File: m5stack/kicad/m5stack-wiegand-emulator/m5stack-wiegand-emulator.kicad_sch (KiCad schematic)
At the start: 42 parts, among them J1 2x15 socket header, J2 2x15 pin header, J3 1x5 female, T1 TestPoint, T2 TestPoint, T3 TestPoint, T4 TestPoint, U1 RP2040, U2 ISOW7841, U3 SN74LVC2G126-EP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

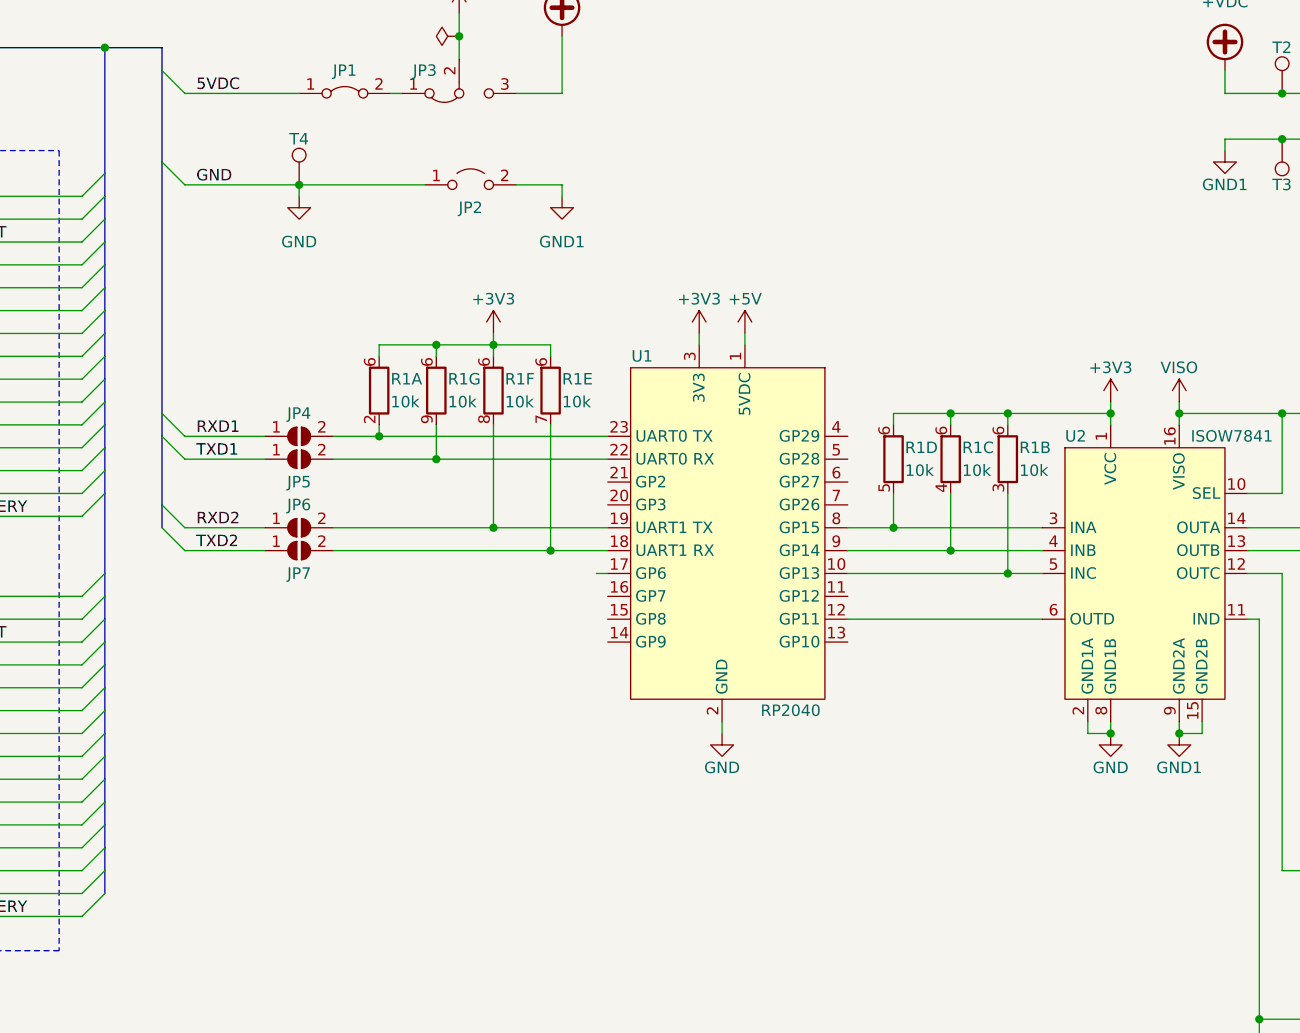
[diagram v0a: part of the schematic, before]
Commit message: M5: moved DI/DO to GP28/29"
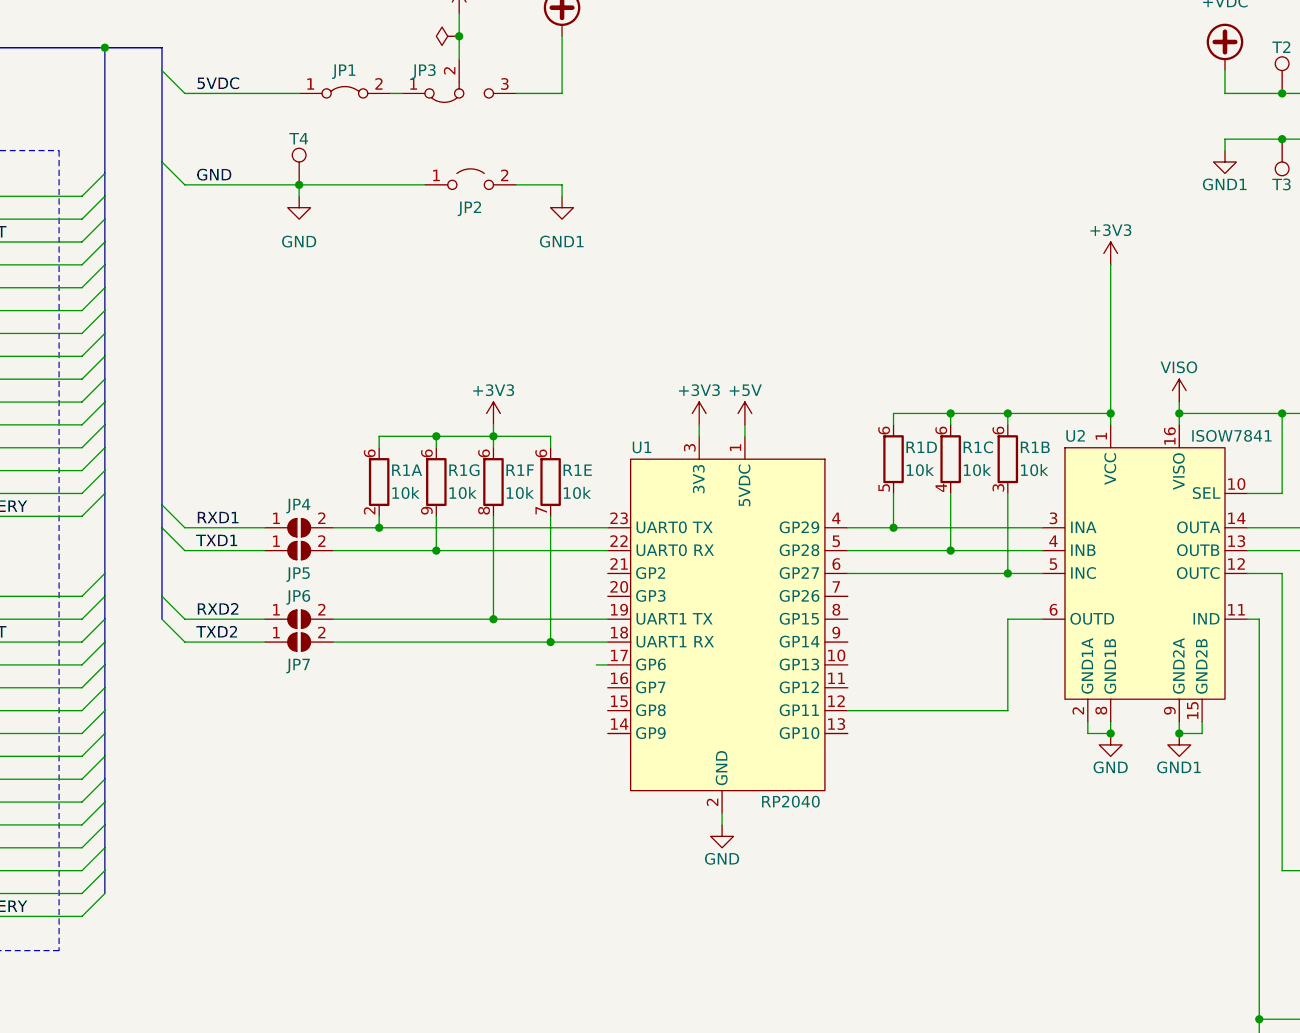
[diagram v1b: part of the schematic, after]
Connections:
- net at R1.4 (R3.2), U2.4 (INB): now also U1.5 (GP28); no longer U1.9 (GP14)
- net at R1.3 (R2.2), U2.5 (INC): now also U1.6 (GP27); no longer U1.10 (GP13)
- net at R1.5 (R4.2), U2.3 (INA): now also U1.4 (GP29); no longer U1.8 (GP15)
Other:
- moved on the sheet: JP4, JP5, JP6, JP7, R1A, R1E, R1F, R1G, U1

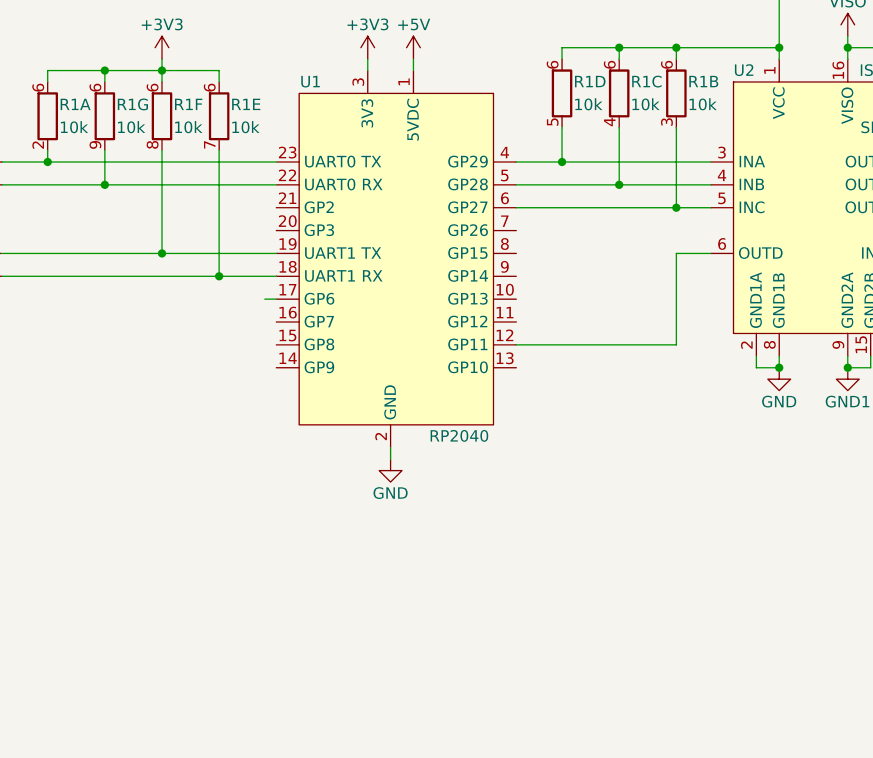
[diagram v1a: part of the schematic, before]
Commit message: M5: routing LED IN signal
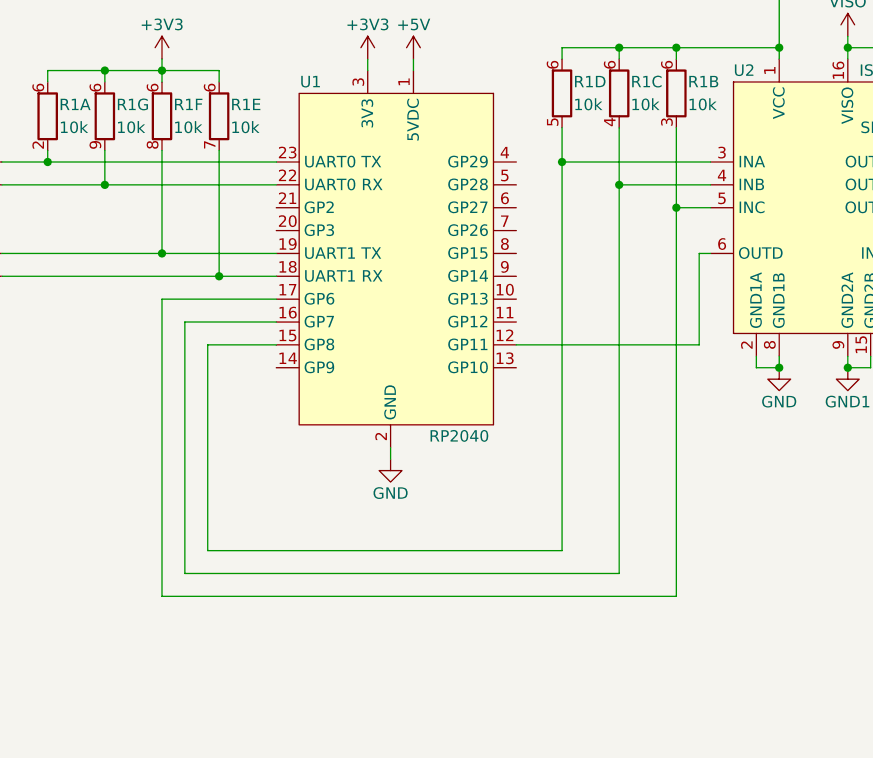
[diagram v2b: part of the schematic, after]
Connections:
- net at R1.4 (R3.2), U2.4 (INB): now also U1.16 (GP7); no longer U1.5 (GP28)
- net at R1.3 (R2.2), U2.5 (INC): now also U1.17 (GP6); no longer U1.6 (GP27)
- net at R1.5 (R4.2), U2.3 (INA): now also U1.15 (GP8); no longer U1.4 (GP29)
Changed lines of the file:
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@@
   (junction (at 233.68 138.43) (diameter 0) (color 0 0 0 0)
   )
+  (junction (at 163.83 88.9) (diameter 0) (color 0 0 0 0)
+  )
   (junction (at 102.87 29.21) (diameter 0) (color 0 0 0 0)
   )
@@
   (junction (at 233.68 148.59) (diameter 0) (color 0 0 0 0)
   )
+  (junction (at 233.68 91.44) (diameter 0) (color 0 0 0 0)
+  )
+  (junction (at 233.68 86.36) (diameter 0) (color 0 0 0 0)
+  )
+  (junction (at 151.13 83.82) (diameter 0) (color 0 0 0 0)
+  )
+  (junction (at 199.39 71.12) (diameter 0) (color 0 0 0 0)
+  )
+  (junction (at 191.77 138.43) (diameter 0) (color 0 0 0 0)
+  )
+  (junction (at 85.09 45.72) (diameter 0) (color 0 0 0 0)
+  )
+  (junction (at 219.71 138.43) (diameter 0) (color 0 0 0 0)
+  )
+  (junction (at 194.31 71.12) (diameter 0) (color 0 0 0 0)
+  )
+  (junction (at 220.98 83.82) (diameter 0) (color 0 0 0 0)
+  )
+  (junction (at 233.68 83.82) (diameter 0) (color 0 0 0 0)
+  )
   (junction (at 157.48 86.36) (diameter 0) (color 0 0 0 0)
   )
-  (junction (at 233.68 91.44) (diameter 0) (color 0 0 0 0)
-  )
-  (junction (at 233.68 86.36) (diameter 0) (color 0 0 0 0)
-  )
-  (junction (at 199.39 71.12) (diameter 0) (color 0 0 0 0)
-  )
-  (junction (at 191.77 138.43) (diameter 0) (color 0 0 0 0)
-  )
-  (junction (at 85.09 45.72) (diameter 0) (color 0 0 0 0)
-  )
-  (junction (at 219.71 138.43) (diameter 0) (color 0 0 0 0)
-  )
-  (junction (at 194.31 71.12) (diameter 0) (color 0 0 0 0)
-  )
-  (junction (at 220.98 83.82) (diameter 0) (color 0 0 0 0)
-  )
-  (junction (at 233.68 83.82) (diameter 0) (color 0 0 0 0)
-  )
   (junction (at 100.33 73.66) (diameter 0) (color 0 0 0 0)
   )
@@
   (junction (at 246.38 138.43) (diameter 0) (color 0 0 0 0)
   )
-  (junction (at 151.13 83.82) (diameter 0) (color 0 0 0 0)
-  )
   (junction (at 106.68 73.66) (diameter 0) (color 0 0 0 0)
   )
   (junction (at 54.61 158.75) (diameter 0) (color 0 0 0 0)
   )
-  (junction (at 163.83 88.9) (diameter 0) (color 0 0 0 0)
-  )
   (bus_entry (at 19.05 93.98) (size 2.54 2.54)
     (stroke (width 0) (type default))
@@
     (stroke (width 0) (type default))
   )
+  (wire (pts (xy 106.68 132.08) (xy 106.68 99.06))
+    (stroke (width 0) (type default))
+  )
   (wire (pts (xy 157.48 71.12) (xy 157.48 72.39))
     (stroke (width 0) (type default))
@@
     (stroke (width 0) (type default))
   )
+  (wire (pts (xy 157.48 129.54) (xy 109.22 129.54))
+    (stroke (width 0) (type default))
+  )
   (wire (pts (xy 157.48 80.01) (xy 157.48 86.36))
     (stroke (width 0) (type default))
@@
     (stroke (width 0) (type default))
   )
-  (wire (pts (xy 119.38 99.06) (xy 118.11 99.06))
+  (wire (pts (xy 106.68 99.06) (xy 119.38 99.06))
     (stroke (width 0) (type default))
   )
@@
     (stroke (width 0) (type default))
   )
+  (wire (pts (xy 163.83 132.08) (xy 106.68 132.08))
+    (stroke (width 0) (type default))
+  )
   (wire (pts (xy 240.03 83.82) (xy 254 83.82))
     (stroke (width 0) (type default))
@@
     (stroke (width 0) (type default))
   )
+  (wire (pts (xy 163.83 88.9) (xy 163.83 132.08))
+    (stroke (width 0) (type default))
+  )
   (wire (pts (xy 219.71 35.56) (xy 222.25 35.56))
     (stroke (width 0) (type default))
   )
+  (wire (pts (xy 111.76 127) (xy 111.76 104.14))
+    (stroke (width 0) (type default))
+  )
   (wire (pts (xy 199.39 78.74) (xy 199.39 88.9))
     (stroke (width 0) (type default))
@@
     (stroke (width 0) (type default))
   )
+  (wire (pts (xy 111.76 104.14) (xy 119.38 104.14))
+    (stroke (width 0) (type default))
+  )
+  (wire (pts (xy 151.13 83.82) (xy 151.13 127))
+    (stroke (width 0) (type default))
+  )
   (wire (pts (xy 182.88 106.68) (xy 185.42 106.68))
     (stroke (width 0) (type default))
@@
     (stroke (width 0) (type default))
   )
-  (wire (pts (xy 163.83 104.14) (xy 163.83 93.98))
+  (wire (pts (xy 166.37 104.14) (xy 166.37 93.98))
     (stroke (width 0) (type default))
   )
@@
     (stroke (width 0) (type default))
   )
-  (wire (pts (xy 163.83 93.98) (xy 167.64 93.98))
+  (wire (pts (xy 166.37 93.98) (xy 167.64 93.98))
     (stroke (width 0) (type default))
   )
@@
     (stroke (width 0) (type default))
   )
+  (wire (pts (xy 157.48 86.36) (xy 157.48 129.54))
+    (stroke (width 0) (type default))
+  )
   (wire (pts (xy 21.59 127) (xy 33.02 127))
     (stroke (width 0) (type default))
@@
     (stroke (width 0) (type default))
   )
-  (wire (pts (xy 146.05 88.9) (xy 163.83 88.9))
-    (stroke (width 0) (type default))
-  )
   (wire (pts (xy 54.61 148.59) (xy 66.04 148.59))
     (stroke (width 0) (type default))
@@
     (stroke (width 0) (type default))
   )
+  (wire (pts (xy 109.22 129.54) (xy 109.22 101.6))
+    (stroke (width 0) (type default))
+  )
   (wire (pts (xy 45.72 93.98) (xy 60.96 93.98))
     (stroke (width 0) (type default))
@@
     (stroke (width 0) (type default))
   )
-  (wire (pts (xy 146.05 86.36) (xy 157.48 86.36))
+  (wire (pts (xy 151.13 127) (xy 111.76 127))
     (stroke (width 0) (type default))
   )
@@
     (stroke (width 0) (type default))
   )
+  (wire (pts (xy 109.22 101.6) (xy 119.38 101.6))
+    (stroke (width 0) (type default))
+  )
   (wire (pts (xy 54.61 148.59) (xy 54.61 151.13))
     (stroke (width 0) (type default))
@@
     (stroke (width 0) (type default))
   )
-  (wire (pts (xy 146.05 104.14) (xy 163.83 104.14))
+  (wire (pts (xy 146.05 104.14) (xy 166.37 104.14))
     (stroke (width 0) (type default))
   )
@@
     (stroke (width 0) (type default))
   )
-  (wire (pts (xy 146.05 83.82) (xy 151.13 83.82))
-    (stroke (width 0) (type default))
-  )

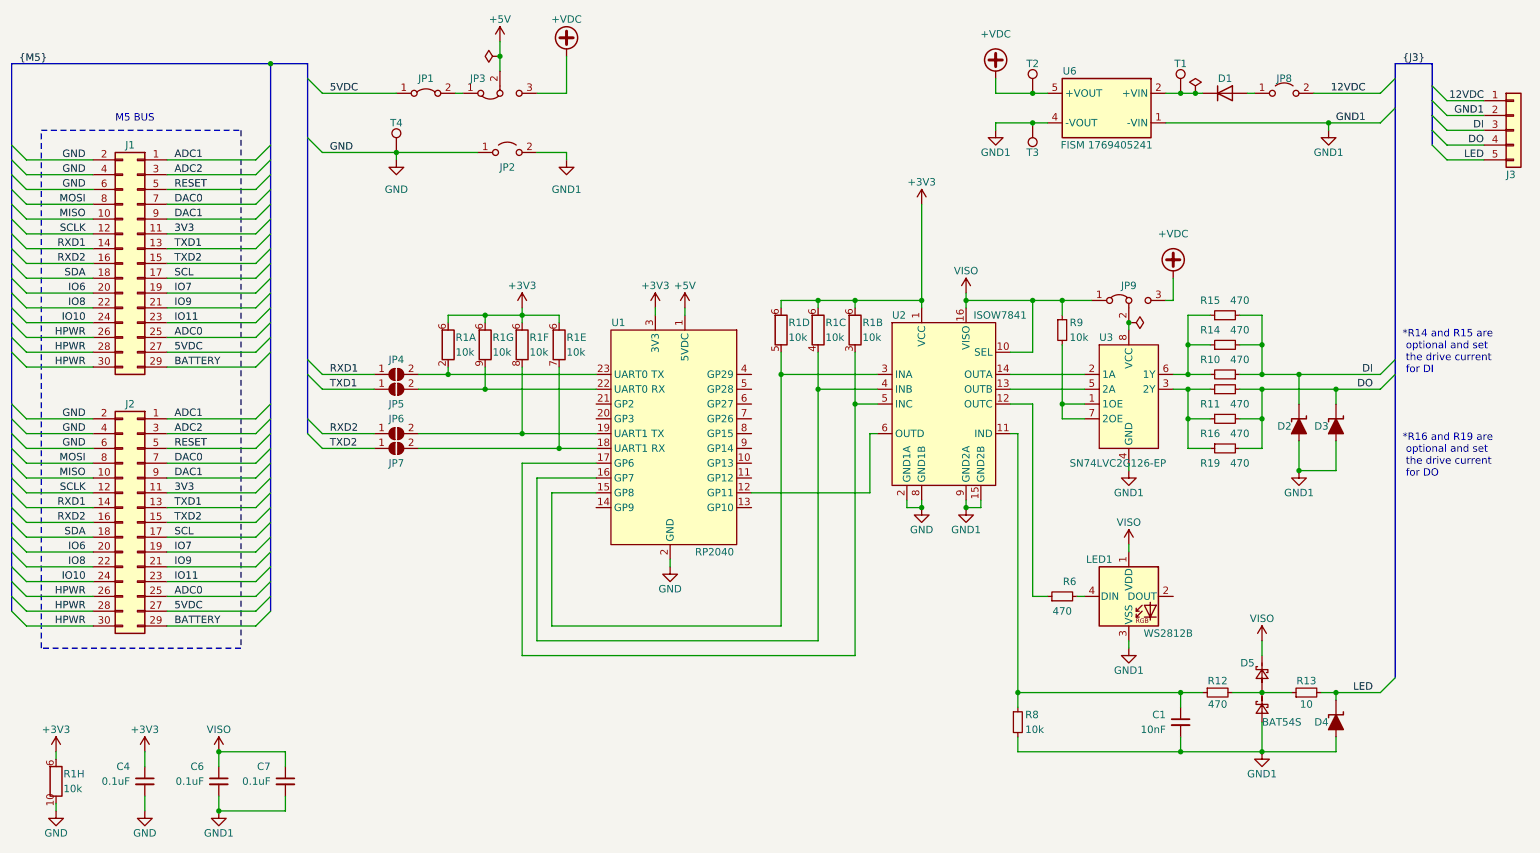
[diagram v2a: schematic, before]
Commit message: M5: rotated U1 and U2 and rerouted
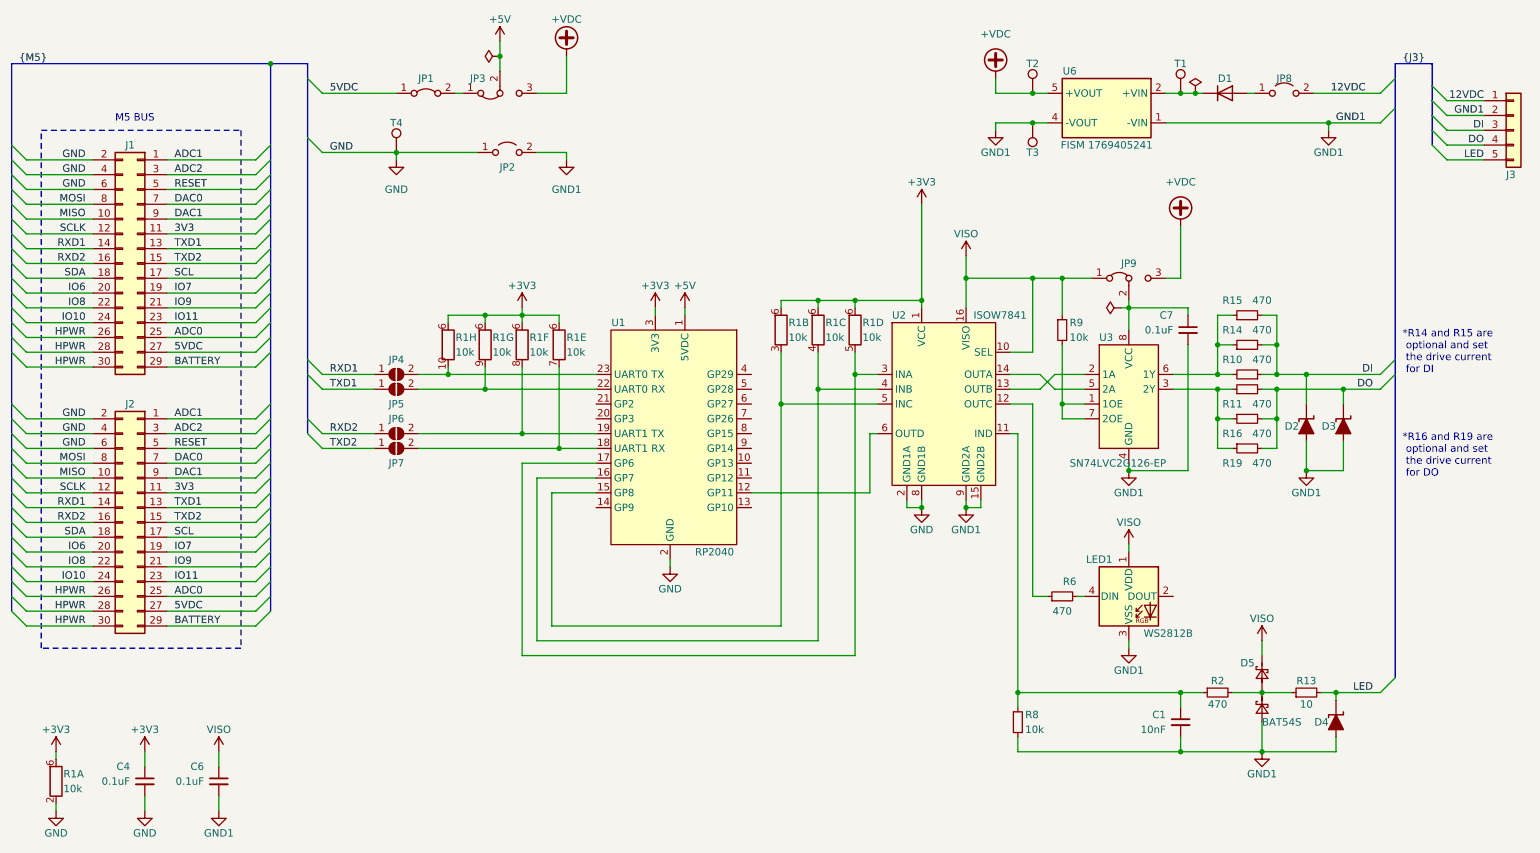
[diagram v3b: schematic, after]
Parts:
- renumbered R12 to R2
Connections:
- net GND: now also R1.2 (R1.2); no longer R1.10 (R8.2)
- net VISO: no longer C7.1
- net at U2.13 (OUTB): now also U3.2 (1A); no longer U3.5 (2A)
- net at U2.14 (OUTA): now also U3.5 (2A); no longer U3.2 (1A)
- net at JP4.2 (B), U1.23 (GP0): now also R1.10 (R8.2); no longer R1.2 (R1.2)
- net at JP9.2 (C), U3.8 (VCC): now also C7.1
- new net: R1.5 (R4.2), U1.17 (GP6), U2.3 (INA)
- new net: R1.3 (R2.2), U1.15 (GP8), U2.5 (INC)
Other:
- moved on the sheet: C7, D2, D3, JP9, R10, R11, R14, R15, R16, R19
